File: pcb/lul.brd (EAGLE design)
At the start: 90 x 96 mm, 77 parts, among them IC1 STM32F072C8T6, IC2 REG1117, IC3 74LVC1G125DBV, U1 UG-2864HSWEG01, X1 USB-MICROB

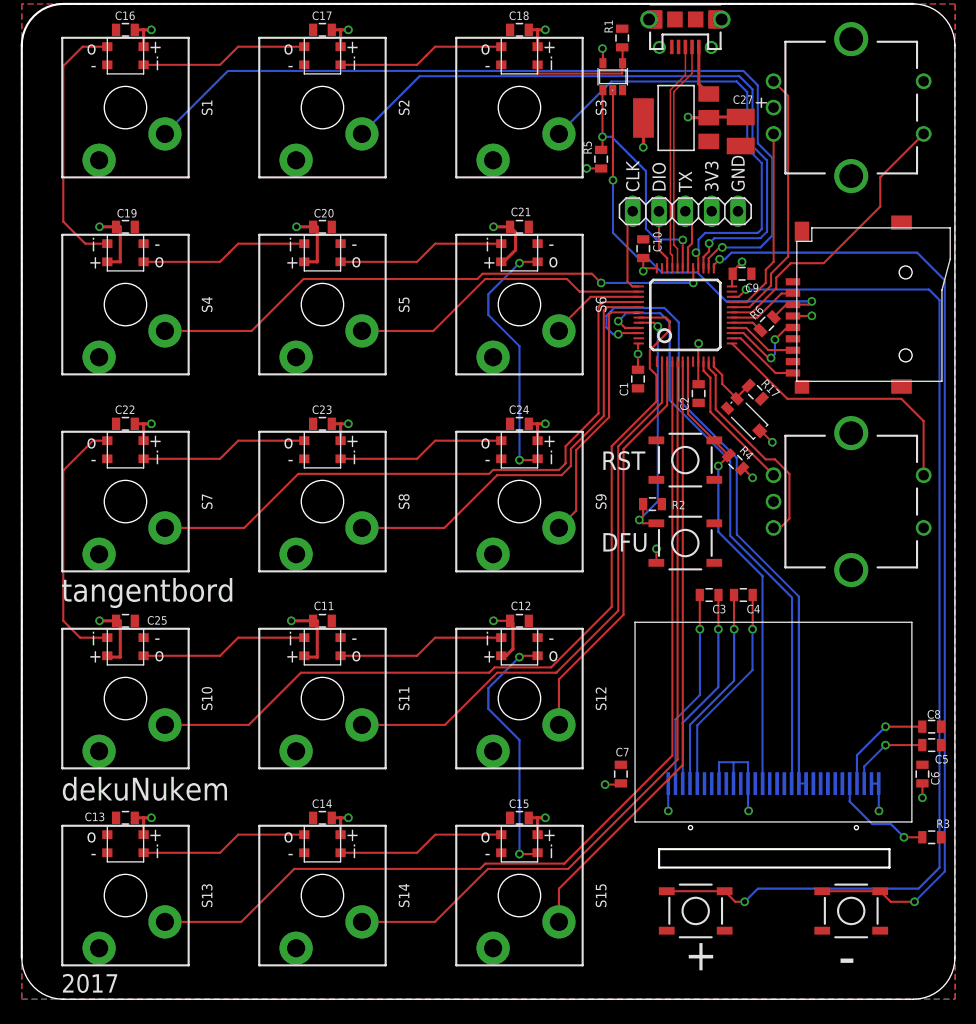
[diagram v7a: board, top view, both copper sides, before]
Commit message: adjusted for both 0.96 and 1.3 inch oled
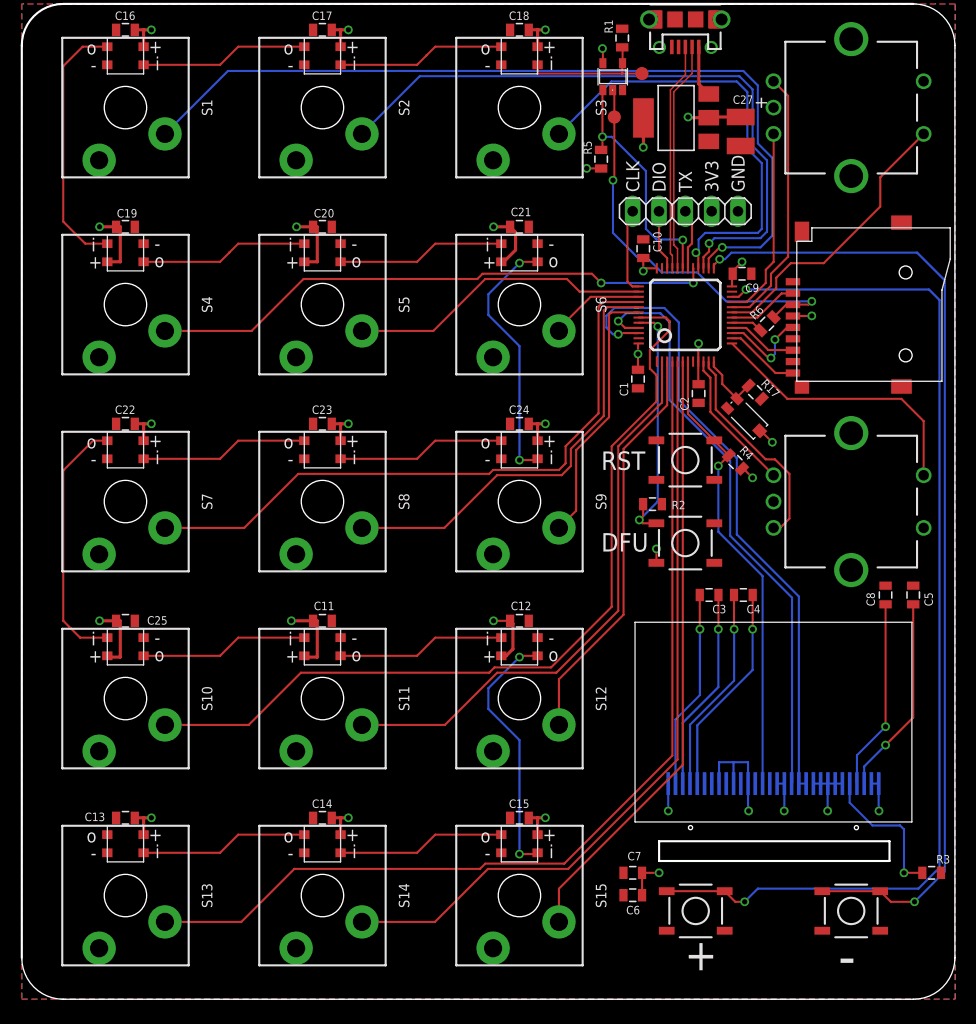
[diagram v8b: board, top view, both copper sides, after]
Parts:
- added TP1, TP2: TEST-POINT3X5, clock:PAD.03X.05
- moved C6 30.3 mm to (58.9, 10.0), turned to 0 degrees
- moved C5 14.6 mm to (86.0, 39.0), turned to 270 degrees
- moved C8 13.5 mm to (83.3, 39.0), turned to 270 degrees
- moved C7 9.59 mm to (58.9, 12.2), turned to 0 degrees
- moved R3 3.43 mm to (87.8, 12.2)
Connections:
- net GND: now also U1.16, U1.17, U1.21, U1.22, U1.23, U1.24, U1.25
- net N$29: now also TP1.P$1
- net SPI_MOSI: now also TP2.P$1
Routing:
- net N$11: track 8.11 -> 19.2 mm
- net GND: track 17.6 -> 26.4 mm, vias 3 -> 5
- net N$12: track 10.2 -> 18.4 mm
- net N$3: track 10.2 -> 14.1 mm
- net N$29: track 11.6 -> 13.5 mm
- net +3V3: track 100.3 -> 101.0 mm, vias 29 -> 28
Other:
- outline, holes or cut-outs redrawn
- board text added: "dekuNukem 2017"
- board text added: "kbord"
- board text removed: "2017"
- board text removed: "dekuNukem"
- board text removed: "tangentbord"
